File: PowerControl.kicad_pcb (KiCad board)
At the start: 2 copper layers, 91 x 76 mm, 26 parts, among them J1 Conn_01x02, J2 Emergency_stop_switch, J3 Emergency_stop_switch, J4 XT60PB-F, J5 XT60PB-M, Q1 IPD80P03P4L-07, Q2 IPD80P03P4L-07, U1 TLP621, U2 TLV76012DBZR

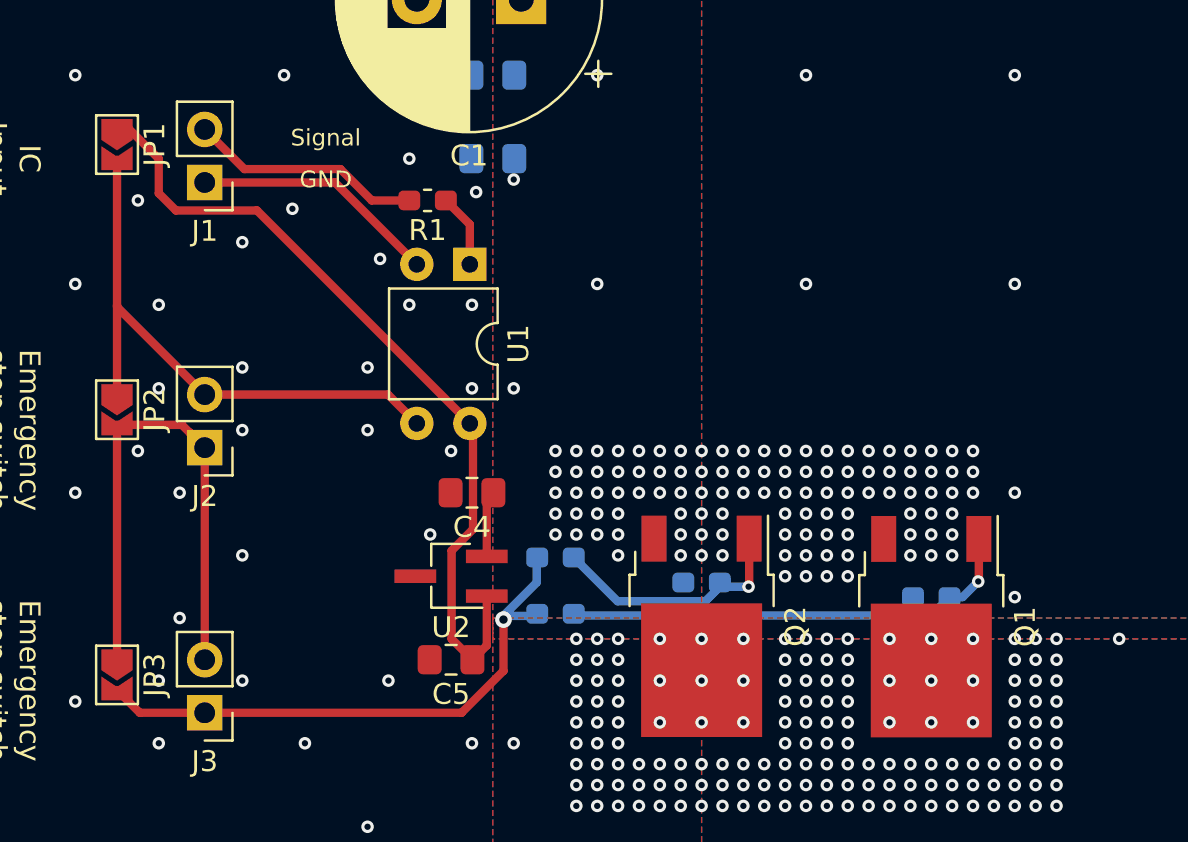
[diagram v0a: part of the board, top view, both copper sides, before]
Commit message: Update: kicad_pcbに修正を変更
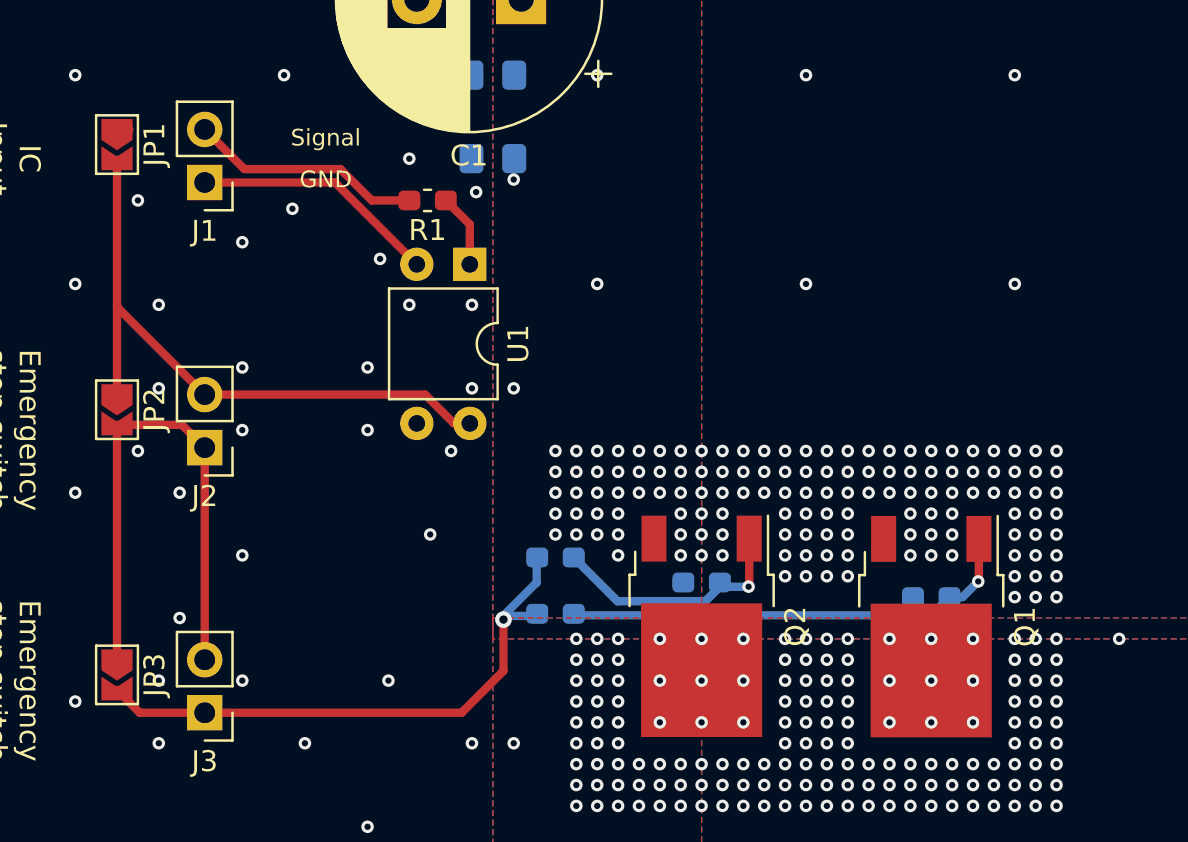
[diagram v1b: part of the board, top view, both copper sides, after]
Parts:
- removed C4, C5: 0.1u, Capacitor_SMD:C_0805_2012Metric_Pad1.15x1.40mm_HandSolder
- removed U2: TLV76012DBZR, Package_TO_SOT_SMD:TSOT-23_HandSoldering
- J2, J3: value Emergency_stop_switch -> EMS_SW
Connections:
- JP1 pad 1: /12V -> GNDPWR
- U1 pad 3: Net-(J2-Pad2) -> GNDPWR
- U1 pad 4: /12V -> Net-(J2-Pad2)
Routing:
- net /12V: track 39.3 -> 0.00 mm
- net VCC: track 3.18 -> 0.00 mm, vias 131 -> 156
- net Net-(J2-Pad2): track 28.0 -> 30.8 mm
- net GNDPWR: track 0.00 -> 0.59 mm

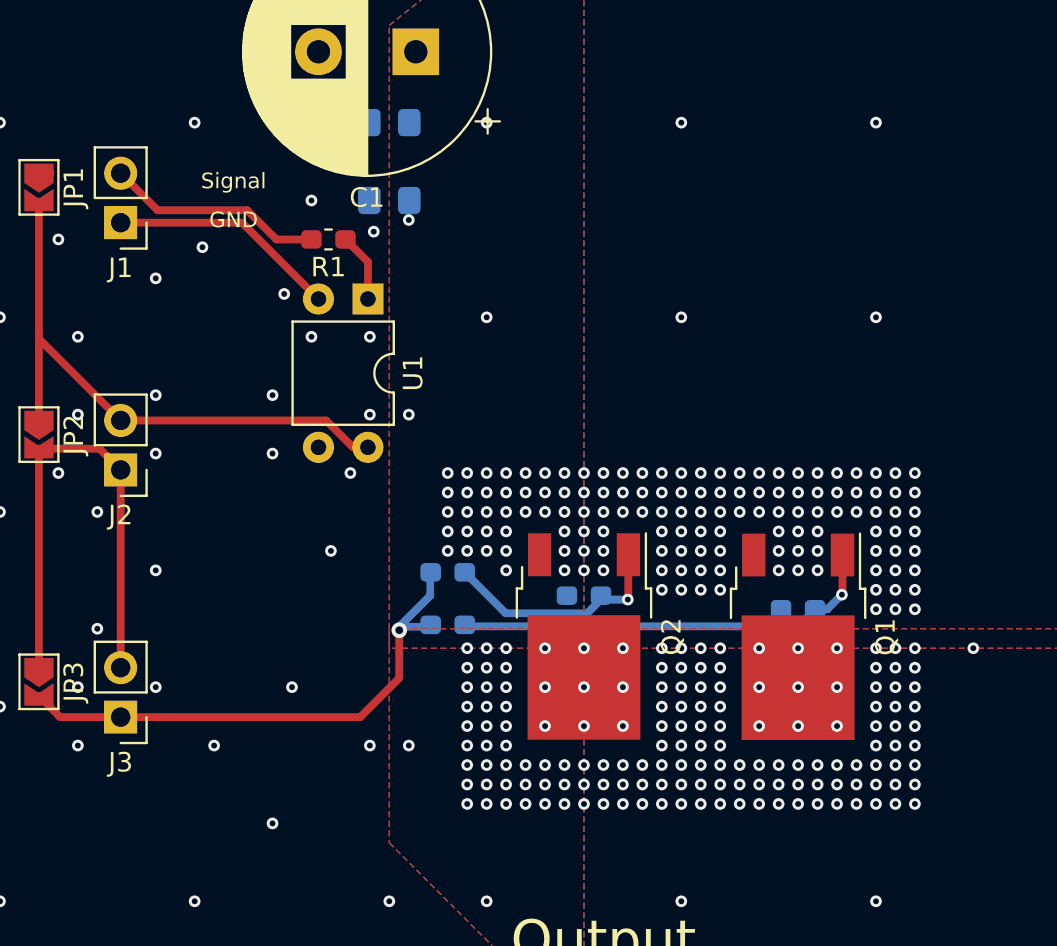
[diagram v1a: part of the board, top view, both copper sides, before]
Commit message: Update: 配線の変更
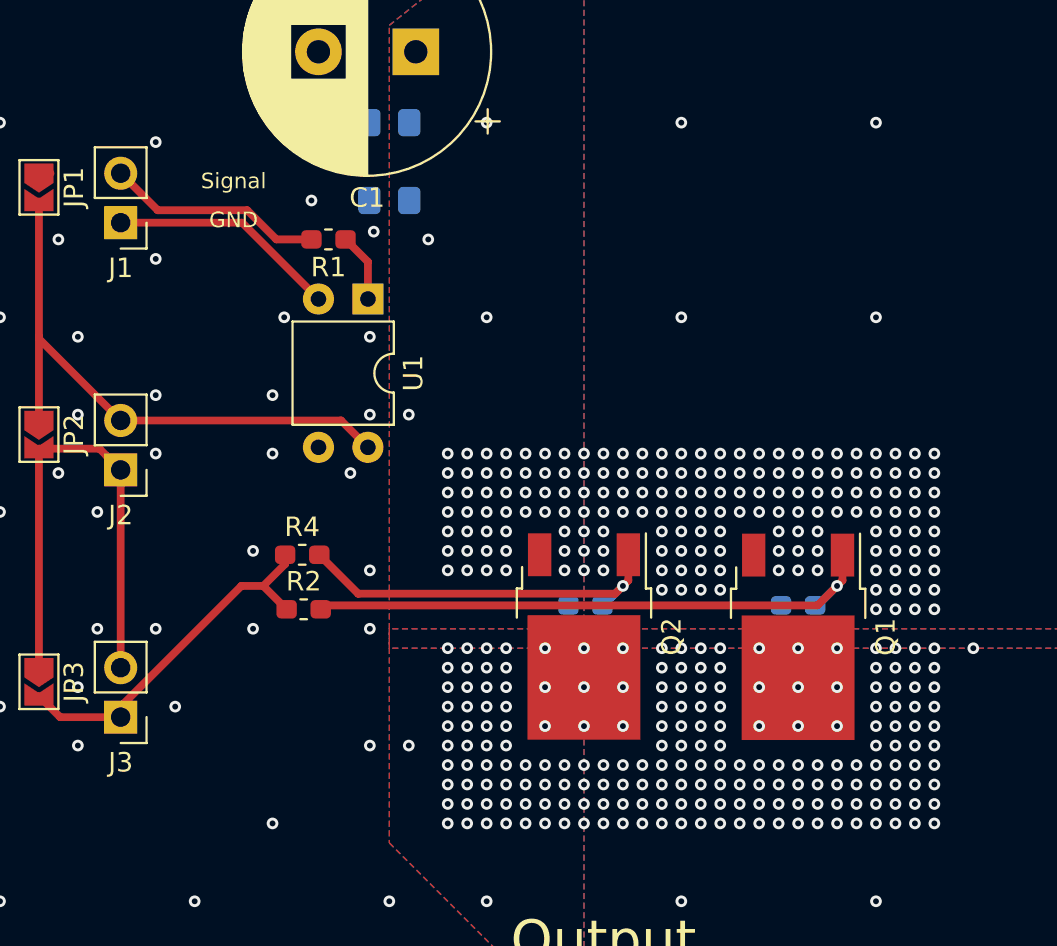
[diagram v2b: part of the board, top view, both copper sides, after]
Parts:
- R2, R4: moved to F.Cu
- moved R4 7.53 mm to (85.5, 112.2)
- moved R2 7.44 mm to (85.6, 115.0)
- moved R5 0.51 mm to (100.1, 114.8)
- moved R3 0.20 mm to (111.0, 114.8)
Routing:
- net Net-(J3-Pad1): track 27.5 -> 18.8 mm, vias 1 -> 0
- net Net-(Q1-Pad1): track 22.1 -> 30.1 mm
- net Net-(Q2-Pad1): track 11.8 -> 19.7 mm
- net VCC: vias 156 -> 193
- net OutPut: vias 163 -> 207
- net GNDPWR: vias 69 -> 68

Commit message: Update: シルクの修正
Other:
- board text added: "EMS SW1"
- board text added: "EMS SW2"
- board text added: "Power controller Version 1.1"
- board text removed: "Emergency stop switch"
- board text removed: "Power controller Version 1.0"
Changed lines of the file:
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@@
     (effects (font (size 1 1) (thickness 0.15)) (justify mirror))
   )
-  (gr_text "IC\nInput" (at 67 94 270) (layer F.SilkS)
+  (gr_text "IC\nInput" (at 69 93 270) (layer F.SilkS)
     (effects (font (size 1 1) (thickness 0.15)))
   )
-  (gr_text "Emergency\nstop switch" (at 67 107 270) (layer F.SilkS)
+  (gr_text "EMS SW1" (at 69 106 -90) (layer F.SilkS)
     (effects (font (size 1 1) (thickness 0.15)))
   )
-  (gr_text "Emergency\nstop switch" (at 67 119 270) (layer F.SilkS)
+  (gr_text "EMS SW2" (at 69 119 -90) (layer F.SilkS)
     (effects (font (size 1 1) (thickness 0.15)))
   )
@@
     (effects (font (size 1 1) (thickness 0.15)))
   )
-  (gr_text "Power controller\nVersion 1.0" (at 70 138) (layer F.SilkS)
+  (gr_text "Power controller\nVersion 1.1" (at 70 138) (layer F.SilkS)
     (effects (font (size 1 1) (thickness 0.15)))
   )

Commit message: Update: 導通確認用のLEDを配置
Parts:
- added D1: LED, LED_SMD:LED_0603_1608Metric_Pad1.05x0.95mm_HandSolder, F.Cu at (133.0, 115.0)
- added D2: LED, LED_SMD:LED_0603_1608Metric_Pad1.05x0.95mm_HandSolder, F.Cu at (133.0, 118.0)
- added R6: R, Resistor_SMD:R_0603_1608Metric_Pad0.98x0.95mm_HandSolder, F.Cu at (127.1, 115.0)
- added R7: R, Resistor_SMD:R_0603_1608Metric_Pad0.98x0.95mm_HandSolder, F.Cu at (127.0, 118.0)
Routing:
- net GNDPWR: track 0.59 -> 48.4 mm, vias 68 -> 69
- net Net-(D2-Pad2): track 0.00 -> 4.21 mm
- net Net-(D1-Pad2): track 0.00 -> 4.12 mm
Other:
- board text added: "https://github.com/picopicodevil/PowerControl/releases"
- board text removed: "https://github.com/picopicodevil/PowerControl.git"
